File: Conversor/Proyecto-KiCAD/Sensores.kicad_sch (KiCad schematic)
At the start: 25 parts, among them U10 OPA365xxD, U7 TMCS1100A4, U8 LM5056APMH/NOPB, U9 ISO7242C

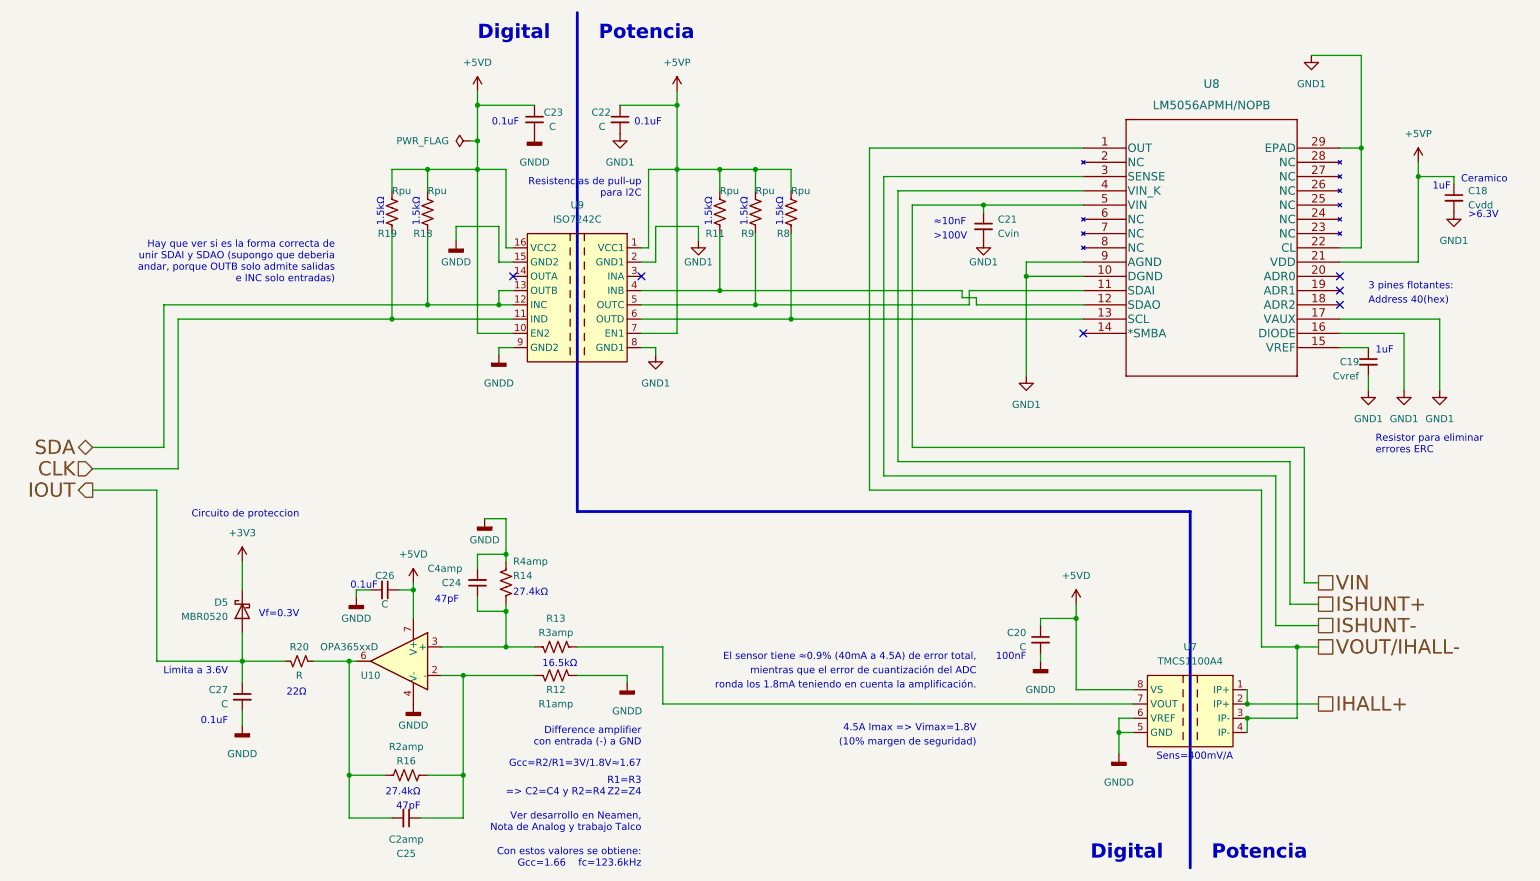
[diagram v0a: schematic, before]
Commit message: Agregar el selector de alim. de 12V y seguir emprolijando la placa
- Agregar modelos de los switches
- Agregar algunos test points
Por hacer:
  - Todo lo de los dos anteriores commits
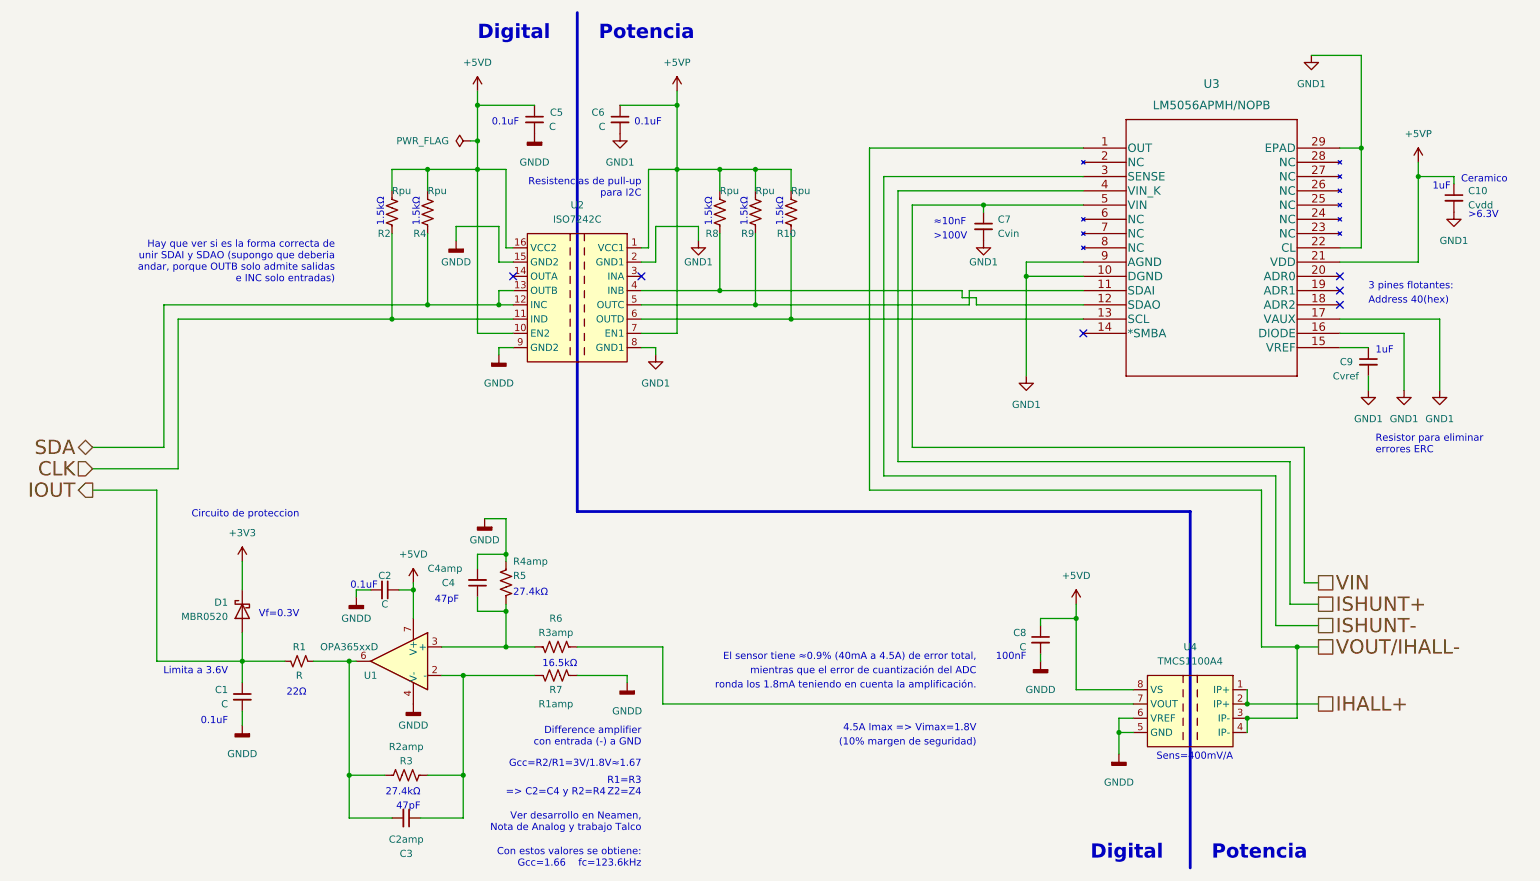
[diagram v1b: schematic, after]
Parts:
- renumbered C27 to C1, C18 to C10, C26 to C2, C25 to C3, C24 to C4, C23 to C5, C22 to C6, C21 to C7, C20 to C8, C19 to C9, D5 to D1, R20 to R1, R8 to R10, R19 to R2, R16 to R3, R18 to R4, R14 to R5, R13 to R6, R12 to R7, R11 to R8, U10 to U1, U9 to U2, U8 to U3, U7 to U4

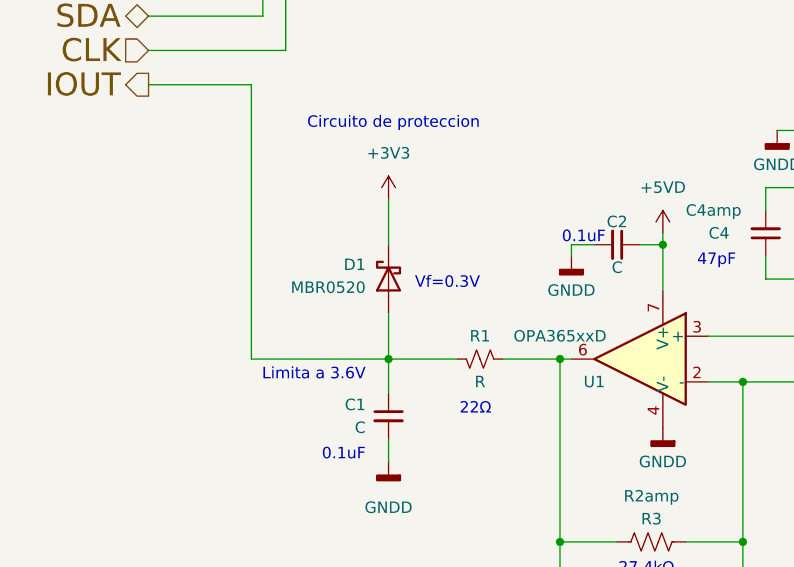
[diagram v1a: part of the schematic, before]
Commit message: Emprolijar la PCB
- Agregar logo de FI
- Redondear pistas faltantes
- Aumentar la distancia del cobre al borde
- acraca racuca
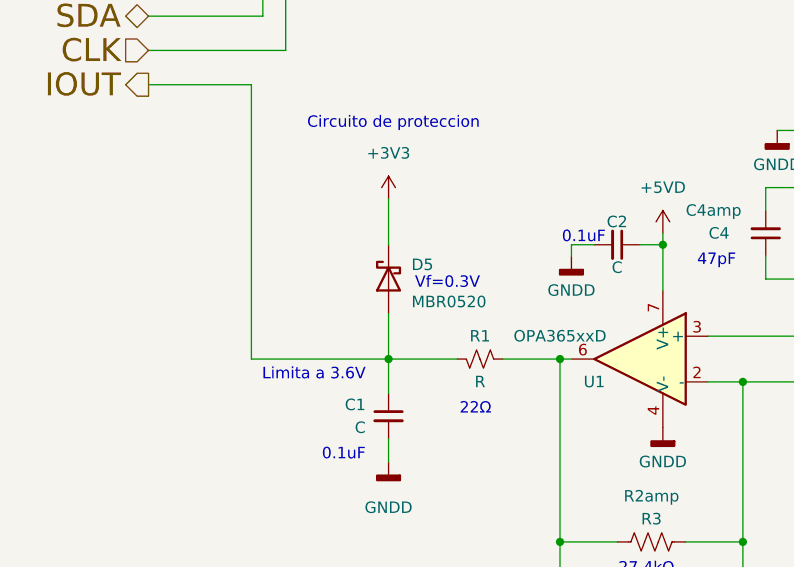
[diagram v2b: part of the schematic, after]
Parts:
- renumbered D1 to D5
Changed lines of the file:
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@@
   )
   (symbol (lib_id "Diode:MBR0520") (at 57.15 119.38 90) (mirror x) (unit 1)
-    (in_bom yes) (on_board yes) (fields_autoplaced)
-    (property "Reference" "D1" (id 0) (at 54.61 117.7924 90)
-      (effects (font (size 1.27 1.27)) (justify left))
+    (in_bom yes) (on_board yes)
+    (property "Reference" "D5" (id 0) (at 59.69 117.7924 90)
+      (effects (font (size 1.27 1.27)) (justify right))
     )
-    (property "Value" "MBR0520" (id 1) (at 54.61 120.3324 90)
-      (effects (font (size 1.27 1.27)) (justify left))
+    (property "Value" "MBR0520" (id 1) (at 59.69 121.92 90)
+      (effects (font (size 1.27 1.27)) (justify right))
     )
     (property "Footprint" "Diode_SMD:D_SOD-123" (id 2) (at 61.595 119.38 0)

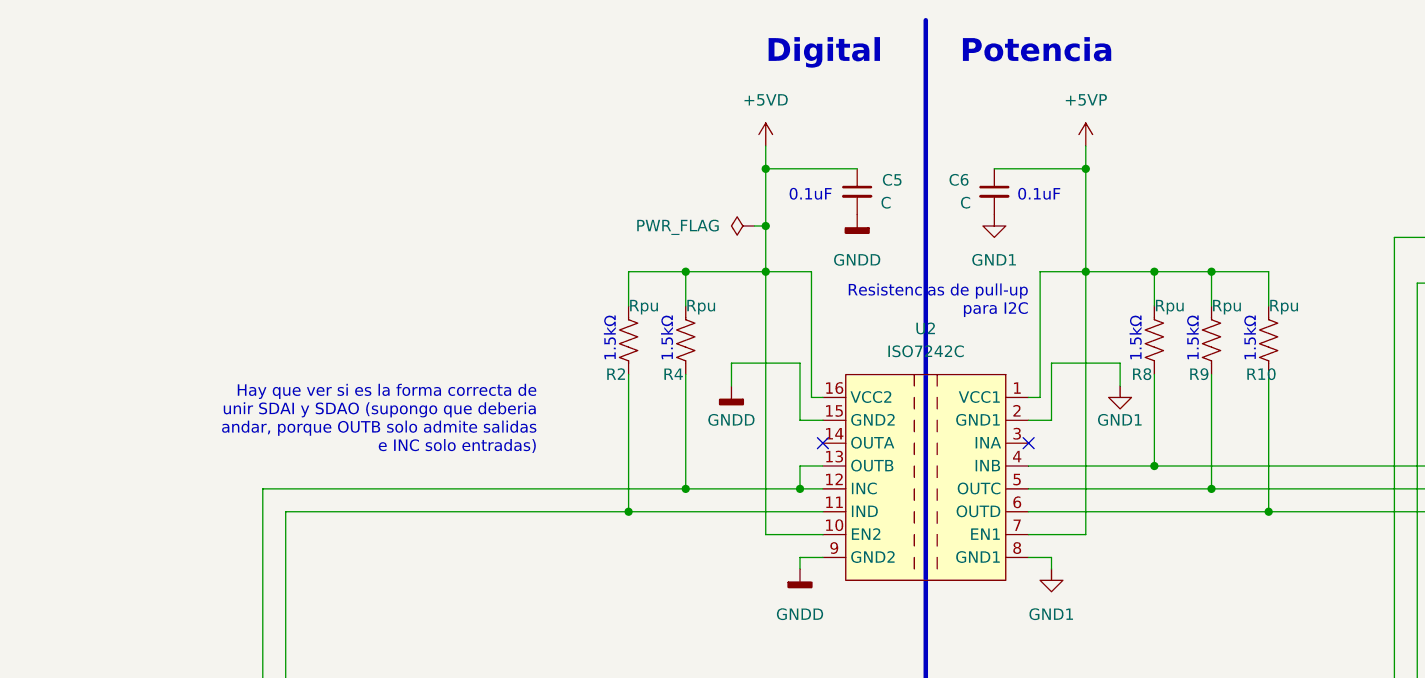
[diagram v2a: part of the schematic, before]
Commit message: Solucionar la union de las lineas de datos I2C
- Segun una evaluation board de Texas, si ya estan separadas las lineas
de I2C como en este caso, solo hay que agregar un adaptador de push-pull
a opne-drain a la salida del aislador
- Se mandó el mail a MayerPCB
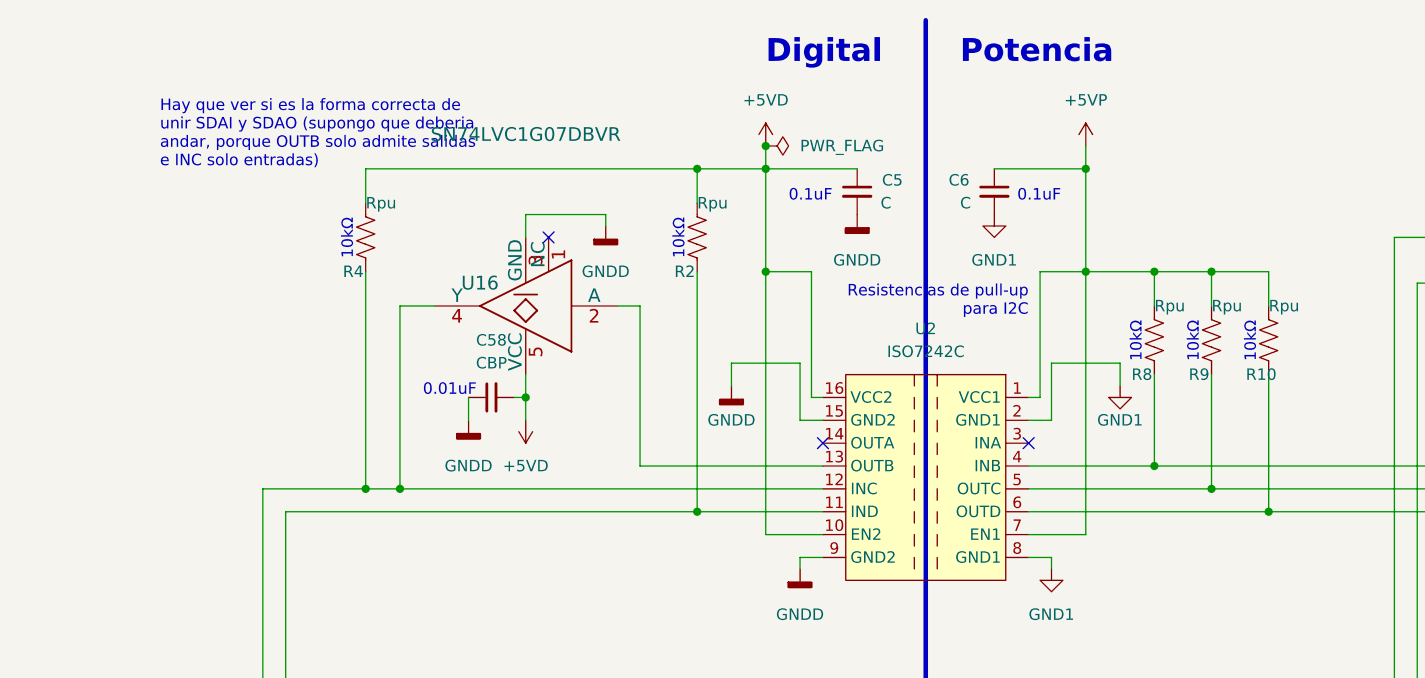
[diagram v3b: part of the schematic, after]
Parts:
- added C58: CBP, Capacitor_SMD:C_1206_3216Metric_Pad1.33x1.80mm_HandSolder, symbol Device:C_Small
- added U16: SN74LVC1G07DBVR, SN74LVC1G07DBVR:SN74LVC1G07DBVR, symbol SN74LVC1G07DBVR:SN74LVC1G07DBVR
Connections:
- net +5VD: now also C58.2, U16.5 (VCC)
- net GNDD: now also C58.1, U16.3 (GND)
- net SDA: now also U16.4 (Y); no longer U2.13 (OUTB)
- new net: U16.2 (A), U2.13 (OUTB)
- no-connect marks 6 -> 7
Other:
- note added: "0.01uF"
- note added: "10kΩ"
- note removed: "1.5kΩ"
- moved on the sheet: R2, R4

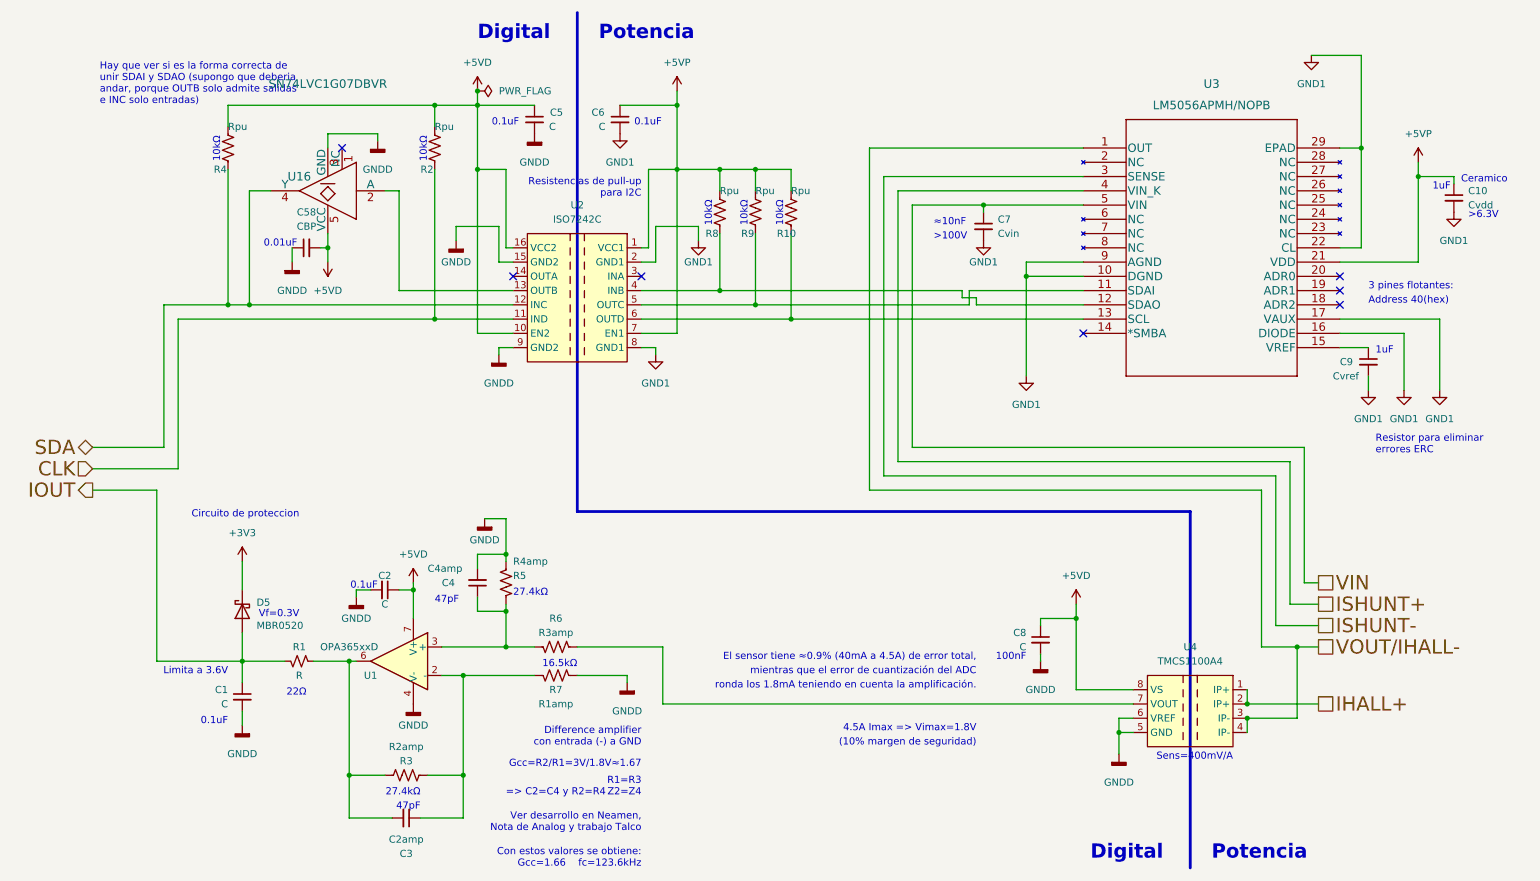
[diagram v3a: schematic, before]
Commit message: Poner el SN74LS06 (inversores open-collector) a la salida del ISO
- Cambiar los planos de cobre de la zona digital:
  - Plano de cobre superior: +5VD
  - Plano de cobre inferior: GNDD
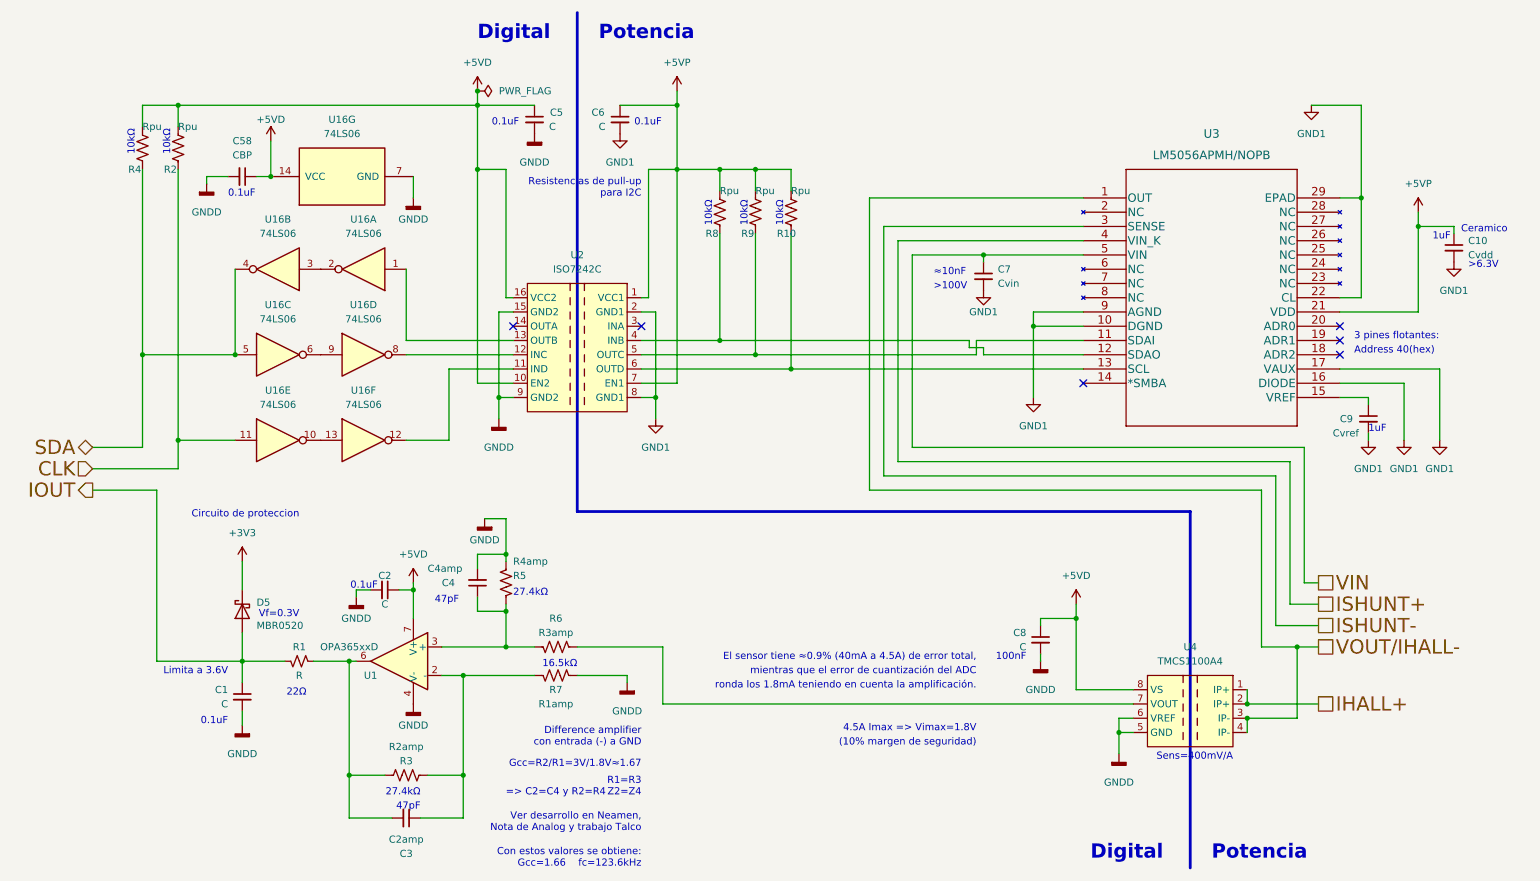
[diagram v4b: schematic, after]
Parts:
- removed U16: SN74LVC1G07DBVR, SN74LVC1G07DBVR:SN74LVC1G07DBVR, symbol SN74LVC1G07DBVR:SN74LVC1G07DBVR
- added U16: 74LS06, symbol 74xx:74LS06
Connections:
- net +5VD: now also C58.1, U16.14 (VCC); no longer C58.2
- net CLK: now also U16.11; no longer U2.11 (IND)
- net GNDD: now also C58.2, U16.7 (GND); no longer C58.1
- net SDA: now also U16.4, U16.5; no longer U2.12 (INC)
- net at U2.13 (OUTB): now also U16.1
- new net: U16.8, U2.12 (INC)
- new net: U16.6, U16.9
- new net: U16.12, U2.11 (IND)
- new net: U16.10, U16.13
- new net: U16.2, U16.3
- no-connect marks 7 -> 6
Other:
- note removed: "0.01uF"
- note removed: "Hay que ver si es la forma correcta de unir SDAI y SDAO (supongo que deberia andar, porque OUTB solo admite salidas e INC solo entradas)"
- note removed: "Resistor para eliminar errores ERC"
- moved on the sheet: C10, C7, C9, R2, R4, U2, U3
